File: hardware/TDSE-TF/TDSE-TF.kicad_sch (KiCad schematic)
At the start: 20 parts, among them J1 Bomba, J2 Sensor_nivel_agua, J4 5VDC-Output, J5 220VAC-Input, J6 Pinera-LCD16x2, M1 Bomba, Q1 IRLZ44, Q2 IRLZ44, U1 STM32F103RBTx

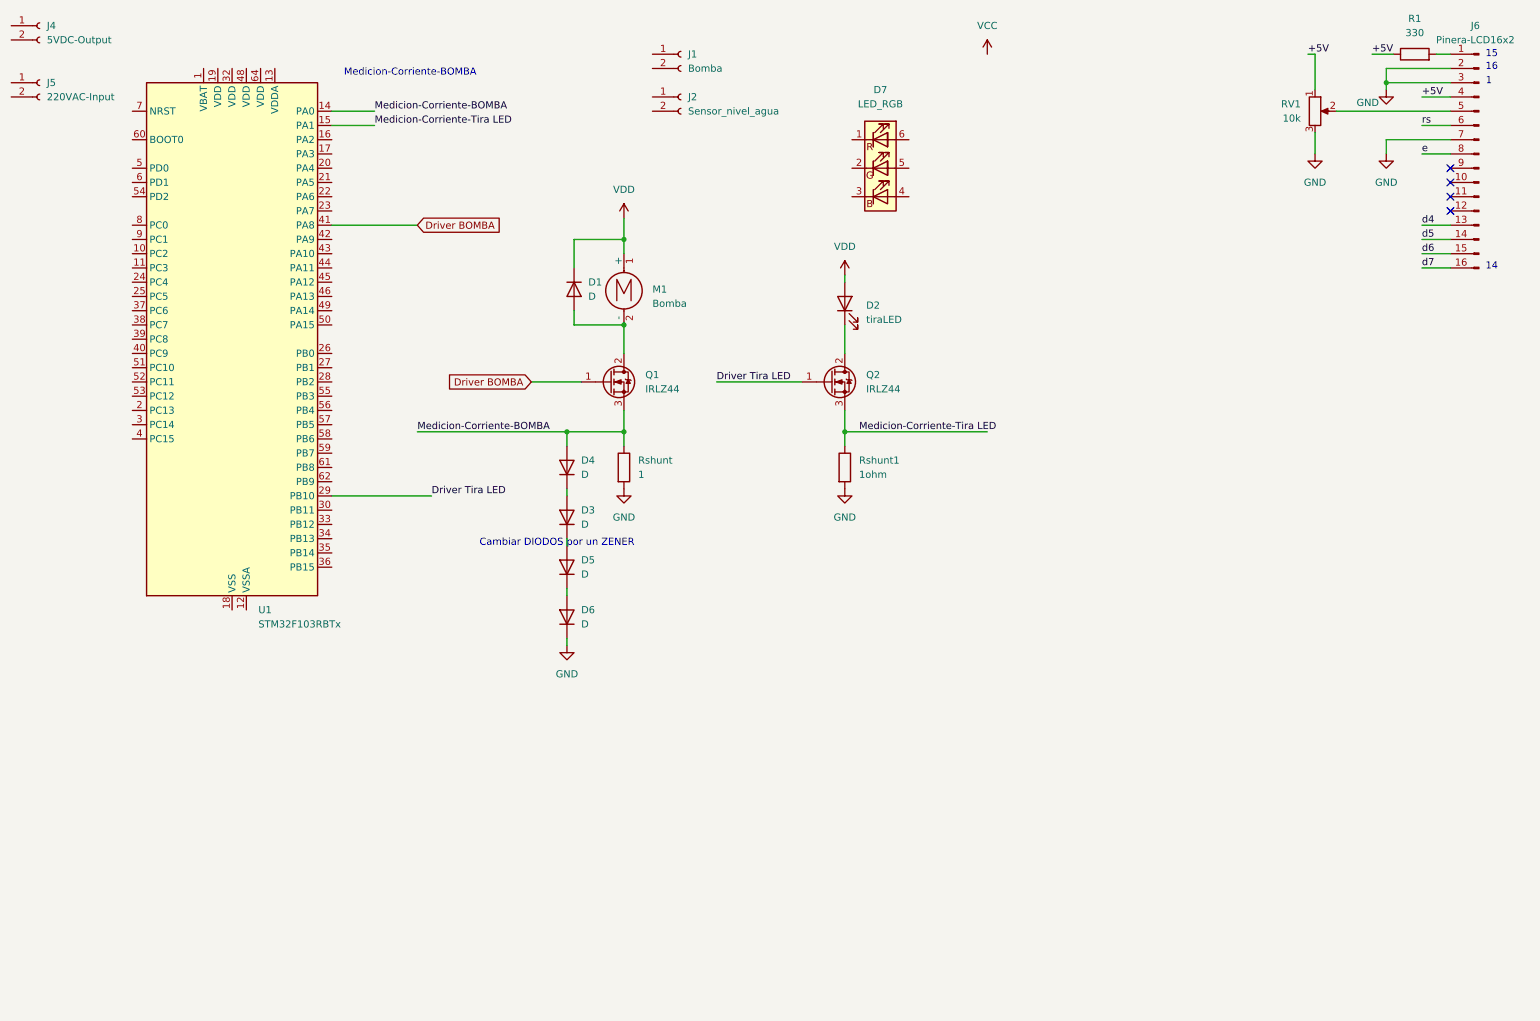
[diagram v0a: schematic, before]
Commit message: Cambios en el esquemático del circuito
Se reemplazó el MCU por las pineras de la placa
Se terminaron varias conexiones (LCD, Sensores, Driver tira LED)
Se emprolijó todo y se añadieron algunas anotaciones en texto
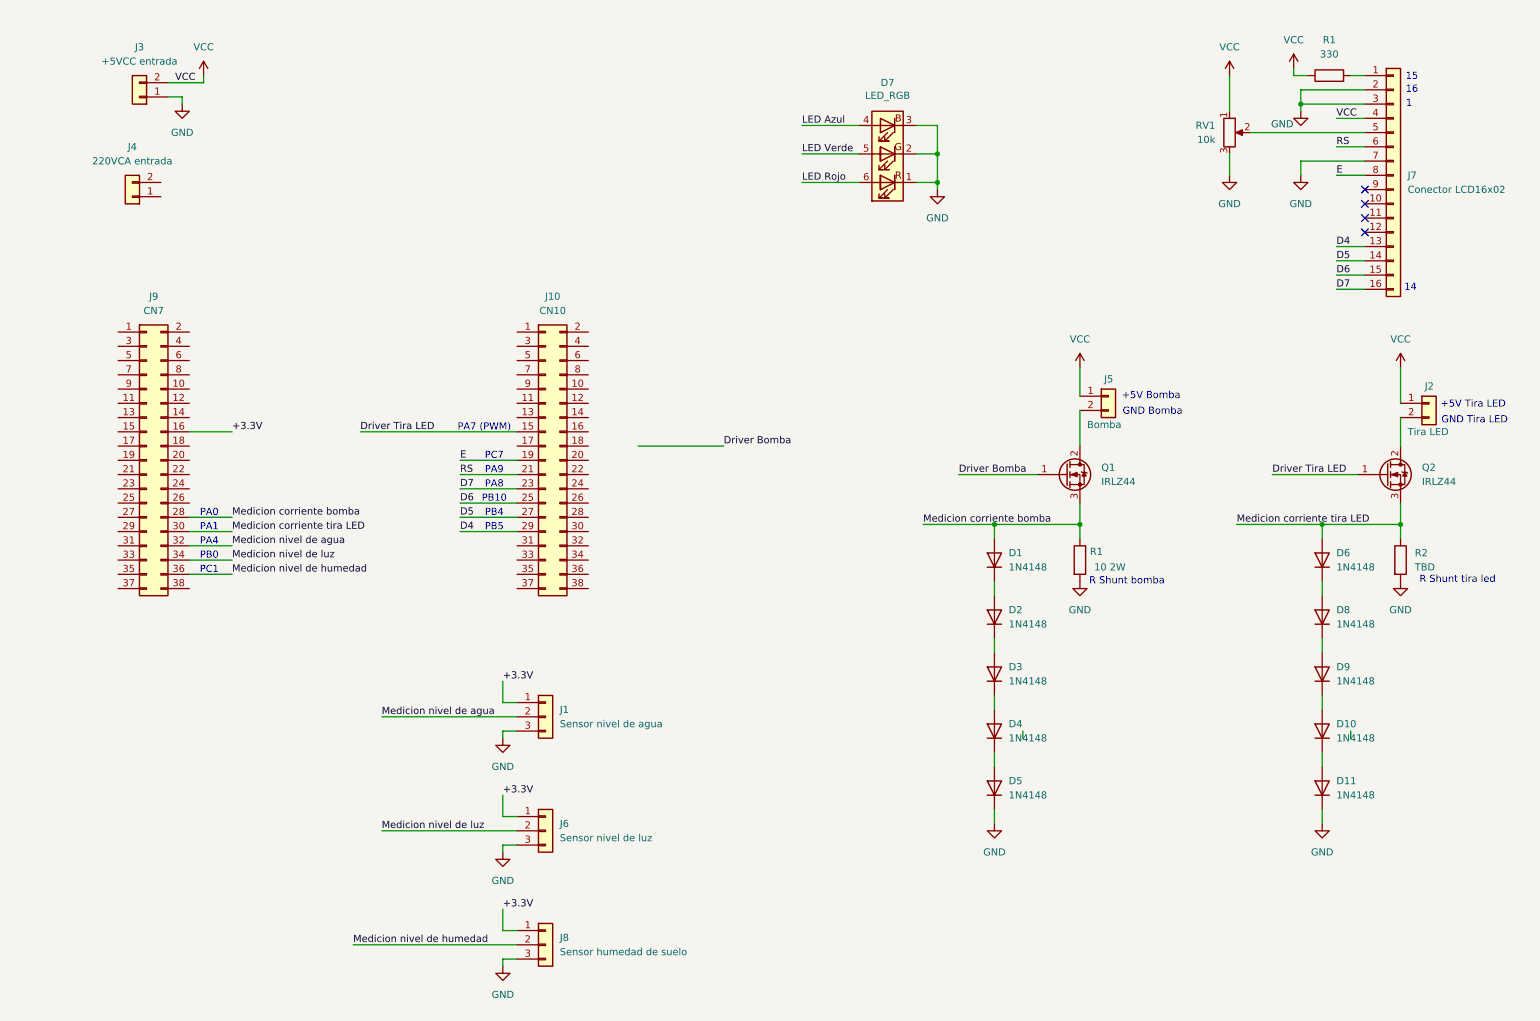
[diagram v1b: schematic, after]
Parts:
- removed D1, D3, D4, D5, D6: D, symbol Device:D
- removed D2: tiraLED, symbol Device:LED
- removed J1: Bomba, symbol Connector:Conn_01x02_Socket
- removed J2: Sensor_nivel_agua, symbol Connector:Conn_01x02_Socket
- removed J4: 5VDC-Output, symbol Connector:Conn_01x02_Socket
- removed J5: 220VAC-Input, symbol Connector:Conn_01x02_Socket
- removed J6: Pinera-LCD16x2, symbol Connector:Conn_01x16_Pin
- removed M1: Bomba, symbol Motor:Motor_DC
- removed U1: STM32F103RBTx, Package_QFP:LQFP-64_10x10mm_P0.5mm, symbol MCU_ST_STM32F1:STM32F103RBTx
- added D1, D10, D11, D2, D3, D4, D5, D6, D8, D9: 1N4148, Diode_THT:D_DO-35_SOD27_P7.62mm_Horizontal, symbol Diode:1N4148
- added J1: Sensor nivel de agua, symbol Connector_Generic:Conn_01x03
- added J10: CN10, symbol Connector_Generic:Conn_02x19_Odd_Even
- added J2: Tira LED, symbol Connector_Generic:Conn_01x02
- added J3: +5VCC entrada, symbol Connector_Generic:Conn_01x02
- added J4: 220VCA entrada, symbol Connector_Generic:Conn_01x02
- added J5: Bomba, symbol Connector_Generic:Conn_01x02
- added J6: Sensor nivel de luz, symbol Connector_Generic:Conn_01x03
- added J7: Conector LCD16x02, symbol Connector_Generic:Conn_01x16
- added J8: Sensor humedad de suelo, symbol Connector_Generic:Conn_01x03
- added J9: CN7, symbol Connector_Generic:Conn_02x19_Odd_Even
- R1: renamed from Rshunt; value 1 -> 10 2W
- R2: renamed from Rshunt1; value 1ohm -> TBD
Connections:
- net +5V is gone; now on net VCC: R1.1, RV1.1
- net Driver Tira LED: now also J10.15 (Pin_15)
- net GND: now also D7.1 (RK), D7.2 (GK), D7.3 (BK), D11.1 (K), D5.1 (K), J1.3 (Pin_3), J3.1 (Pin_1), J6.3 (Pin_3), J7.2 (Pin_2), J7.3 (Pin_3), J7.7 (Pin_7), J8.3 (Pin_3)
- net VCC: now also J2.1 (Pin_1), J3.2 (Pin_2), J5.1 (Pin_1), J7.4 (Pin_4)
- net at Q1.2 (D): now also J5.2 (Pin_2)
- net at Q2.2 (D): now also J2.2 (Pin_2)
- net at RV1.2: now also J7.5 (Pin_5)
- net at R1.2: now also J7.1 (Pin_1)
- net LED Azul: now reaches D7.4 (BA)
- net LED Verde: now reaches D7.5 (GA)
- net LED Rojo: now reaches D7.6 (RA)
- net Driver BOMBA renamed Driver Bomba
- net Medicion-Corriente-BOMBA renamed Medicion corriente bomba
- net Medicion corriente bomba: now also D1.2 (A), J9.28 (Pin_28)
- net Medicion-Corriente-Tira LED renamed Medicion corriente tira LED
- net Medicion corriente tira LED: now also D6.2 (A), J9.30 (Pin_30)
- new net: D6.1 (K), D8.2 (A)
- new net: D10.1 (K), D11.2 (A)
- new net: D10.2 (A), D9.1 (K)
- new net: D1.1 (K), D2.2 (A)
- new net: D8.1 (K), D9.2 (A)
- new net: D4.1 (K), D5.2 (A)
- new net: D3.1 (K), D4.2 (A)
- new net: D2.1 (K), D3.2 (A)
- new net +3.3V: J1.1 (Pin_1), J6.1 (Pin_1), J8.1 (Pin_1), J9.16 (Pin_16)
- new net D4: J10.29 (Pin_29), J7.13 (Pin_13)
- new net D5: J10.27 (Pin_27), J7.14 (Pin_14)
- new net D6: J10.25 (Pin_25), J7.15 (Pin_15)
- new net D7: J10.23 (Pin_23), J7.16 (Pin_16)
- new net E: J10.19 (Pin_19), J7.8 (Pin_8)
- new net Medicion nivel de agua: J1.2 (Pin_2), J9.32 (Pin_32)
- new net Medicion nivel de humedad: J8.2 (Pin_2), J9.36 (Pin_36)
- new net Medicion nivel de luz: J6.2 (Pin_2), J9.34 (Pin_34)
- new net RS: J10.21 (Pin_21), J7.6 (Pin_6)
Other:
- note added: "+5V Bomba"
- note added: "+5V Tira LED"
- note added: "GND Bomba"
- note added: "GND Tira LED"
- note added: "PA0"
- note added: "PA1"
- note added: "PA4"
- note added: "PA7 (PWM)"
- note added: "PA8"
- note added: "PA9"
- note added: "PB0"
- note added: "PB10"
- note added: "PB4"
- note added: "PB5"
- note added: "PC1"
- note added: "PC7"
- note added: "R Shunt bomba"
- note added: "R Shunt tira led"
- note removed: "Cambiar DIODOS por un ZENER"
- note removed: "Medicion-Corriente-BOMBA"
- moved on the sheet: D7, Q1, Q2, R1, R2, RV1

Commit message: Finalizada primera versión de circuito esquematico
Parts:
- removed D7: LED_RGB, symbol Device:LED_RGB
- added BZ1: Buzzer, symbol Device:Buzzer
- added D11: LED_RGB, LED_SMD:LED_Inolux_IN-P55TATRGB_PLCC6_5.0x5.5mm_P1.8mm, symbol LED:Inolux_IN-P55TATRGB
- added J11: 220VCA salida, symbol Connector_Generic:Conn_01x02
- added R4, R5, R6, R7: 10k, symbol Device:R
- added SW1: Enter, symbol Switch:SW_Push
- added SW2: Anterior, symbol Switch:SW_Push
- added SW3: Siguiente, symbol Switch:SW_Push
- added SW4: Escape, symbol Switch:SW_Push
- added U1: AM2302, Sensor:ASAIR_AM2302_P2.54mm_Vertical, symbol Sensor:AM2302
- R1: footprint (none) -> Resistor_THT:R_Axial_DIN0617_L17.0mm_D6.0mm_P25.40mm_Horizontal
- renumbered D11 to D10, D8 to D7, D9 to D8, D10 to D9, R1 to R3
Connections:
- net +3.3V: now also U1.1 (VDD)
- net Driver Bomba: now also J10.31 (Pin_31)
- net Driver Tira LED: now also J10.17 (Pin_17); no longer J10.15 (Pin_15)
- net GND: now also BZ1.2 (-), D11.1 (KB), D11.2 (KR), D11.3 (KG), SW1.2, SW2.2, SW3.2, SW4.2, U1.4 (GND)
- net LED Azul: now also J10.15 (Pin_15), D11.6 (AB)
- net LED Rojo: now also J10.13 (Pin_13), D11.5 (AR)
- net LED Verde: now also J10.11 (Pin_11), D11.4 (AG)
- net VCC: now also R4.2, R5.2, R6.2, R7.2
- net Medicion DHT22 (AM2302): now reaches J10.22 (Pin_22)
- net Medicion DHT22 (AM2302): now also U1.2 (SDA)
- net Boton Siguiente: now reaches J10.24 (Pin_24)
- net Boton Siguiente: now also R6.1, SW3.1
- net Boton Anterior: now reaches J10.26 (Pin_26)
- net Boton Anterior: now also R5.1, SW2.1
- net Boton Enter: now reaches J10.28 (Pin_28)
- net Boton Enter: now also R4.1, SW1.1
- net Boton Escape: now reaches J10.30 (Pin_30)
- net Boton Escape: now also R7.1, SW4.1
- net Buzzer: now reaches J10.33 (Pin_33)
- net Buzzer: now also BZ1.1 (+)
- net at J4.1 (Pin_1): now also J11.2 (Pin_2)
- net at J4.2 (Pin_2): now also J11.1 (Pin_1)
- no-connect marks 4 -> 57
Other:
- note added: "PA10"
- note added: "PA5 (PWM)"
- note added: "PA6 (PWM)"
- note added: "PB1"
- note added: "PB13"
- note added: "PB14"
- note added: "PB15"
- note added: "PB2"
- note added: "PB3 (PWM)"
- note added: "PB6 (PWM)"
- company: (none) -> FIUBA - TDSE
- title: (none) -> Placa base Smartceta
- moved on the sheet: D1, D10, D2, D3, D4, D5, D6, D7, D8, D9, J1, J10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
